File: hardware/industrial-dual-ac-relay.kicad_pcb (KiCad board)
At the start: 2 copper layers, 40 x 40 mm, 29 parts, among them P1 CON-SENSOR, P2 Digital Output, P3 Debug, P4 Boot, U1 XMC1100, U2 AQH3213AX, U5 AQH3213AX, U6 DRILL, U7 DRILL, U8 DRILL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

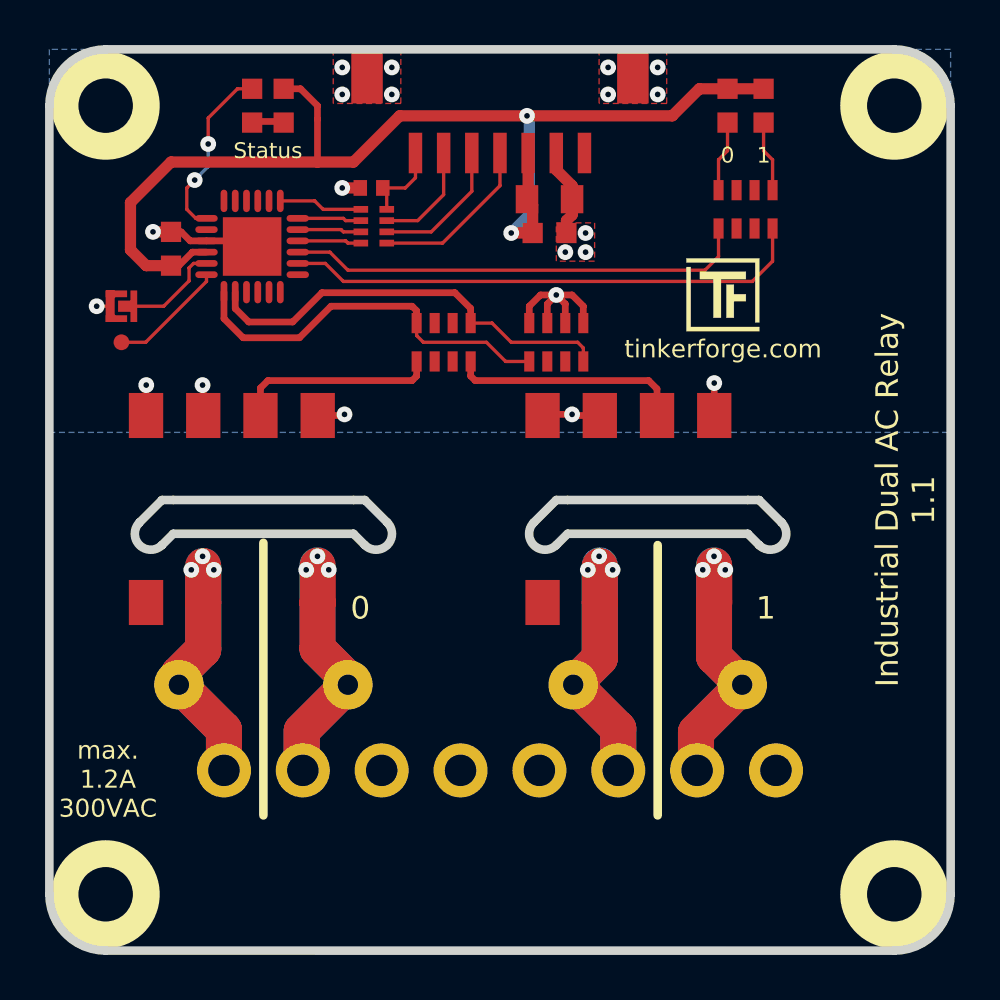
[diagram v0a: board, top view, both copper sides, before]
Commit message: changed to KiCad 6, changed OQ footprint for more clearence
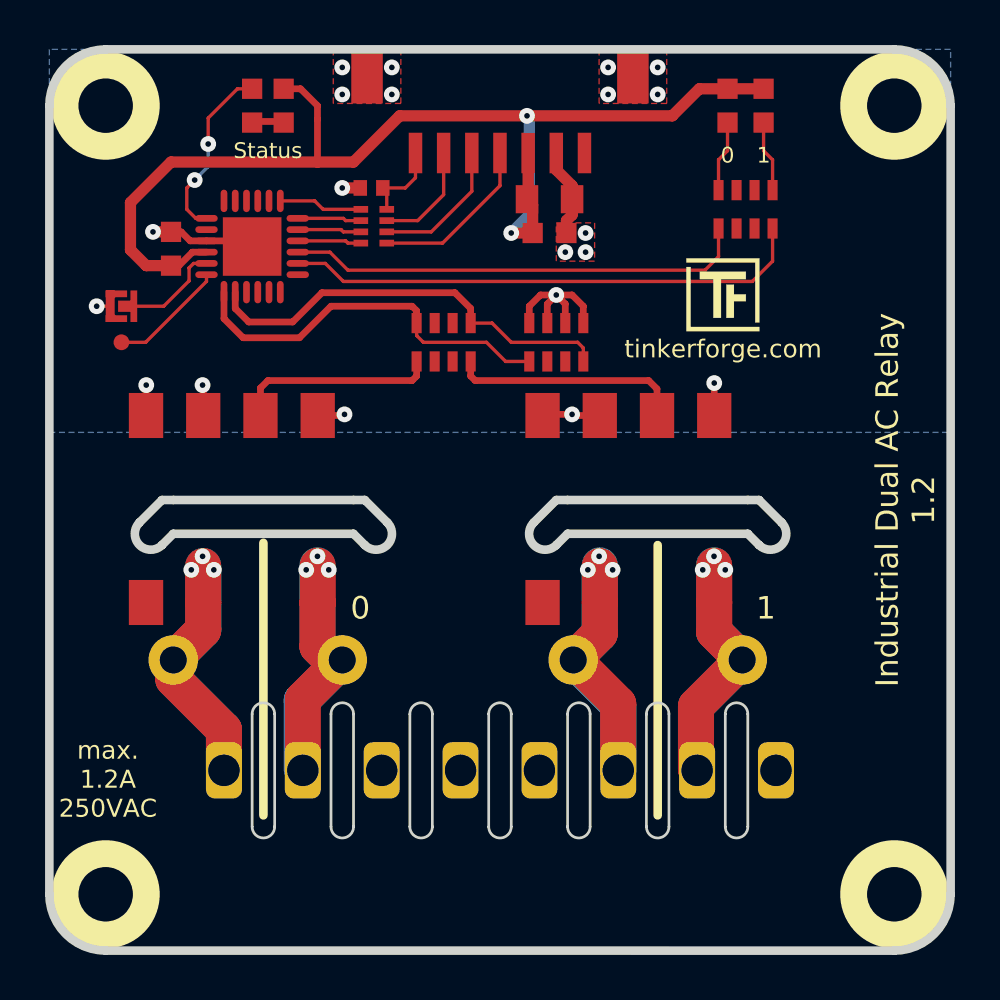
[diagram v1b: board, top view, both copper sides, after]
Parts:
- P2: footprint kicad-libraries:OQ_8P -> kicad-libraries:OQ_8P_230V
- moved R4 1.13 mm to (107.0, 65.2)
- moved R1 1.10 mm to (124.8, 65.2)
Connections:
- P1 pad 1: Net-(P1-Pad1) -> unconnected-(P1-Pad1)
- P2 pad 3: Net-(P2-Pad3) -> unconnected-(P2-Pad3)
- P2 pad 4: Net-(P2-Pad4) -> unconnected-(P2-Pad4)
- P2 pad 5: Net-(P2-Pad5) -> unconnected-(P2-Pad5)
- P2 pad 8: Net-(P2-Pad8) -> unconnected-(P2-Pad8)
- RP1 pad 2: Net-(RP1-Pad2) -> unconnected-(RP1-Pad2)
- RP1 pad 3: Net-(RP1-Pad3) -> unconnected-(RP1-Pad3)
- RP1 pad 6: Net-(RP1-Pad6) -> unconnected-(RP1-Pad6)
- RP1 pad 7: Net-(RP1-Pad7) -> unconnected-(RP1-Pad7)
- RP3 pad 2: Net-(RP3-Pad2) -> unconnected-(RP3-Pad2)
- RP3 pad 3: Net-(RP3-Pad3) -> unconnected-(RP3-Pad3)
- RP3 pad 6: Net-(RP3-Pad6) -> unconnected-(RP3-Pad6)
- RP3 pad 7: Net-(RP3-Pad7) -> unconnected-(RP3-Pad7)
- RP4 pad 2: Net-(RP4-Pad2) -> unconnected-(RP4-Pad2)
- RP4 pad 3: Net-(RP4-Pad3) -> unconnected-(RP4-Pad3)
- U1 pad 15: Net-(U1-Pad15) -> unconnected-(U1-Pad15)
- U1 pad 16: Net-(U1-Pad16) -> unconnected-(U1-Pad16)
- U1 pad 17: Net-(U1-Pad17) -> unconnected-(U1-Pad17)
- U1 pad 18: Net-(U1-Pad18) -> unconnected-(U1-Pad18)
- U1 pad 19: Net-(U1-Pad19) -> unconnected-(U1-Pad19)
- U1 pad 2: Net-(U1-Pad2) -> unconnected-(U1-Pad2)
- U1 pad 3: Net-(U1-Pad3) -> unconnected-(U1-Pad3)
- U1 pad 4: Net-(U1-Pad4) -> unconnected-(U1-Pad4)
- U1 pad 5: Net-(U1-Pad5) -> unconnected-(U1-Pad5)
- U1 pad 6: Net-(U1-Pad6) -> unconnected-(U1-Pad6)
- U1 pad 8: Net-(U1-Pad8) -> unconnected-(U1-Pad8)
- U2 pad 5: Net-(U2-Pad5) -> unconnected-(U2-Pad5)
- U5 pad 5: Net-(U5-Pad5) -> unconnected-(U5-Pad5)
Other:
- net class Default removed
- board text added: "Industrial Dual AC Relay 1.2"
- board text added: "max. 1.2A 250VAC"
- board text removed: "Industrial Dual AC Relay 1.1"
- board text removed: "max. 1.2A 300VAC"

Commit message: changes
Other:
- board text added: "max. 1.2A 230VAC"
- board text removed: "max. 1.2A 250VAC"
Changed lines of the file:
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@@
       (effects (font (size 0.59944 0.59944) (thickness 0.12446)))
     )
-    (fp_line (start 7.5 -2.5) (end 7.5 2.5) (layer "Edge.Cuts") (width 0.12))
+    (fp_line (start 7.5 -5) (end 7.5 2.5) (layer "Edge.Cuts") (width 0.12))
     (fp_line (start 3 -2.5) (end 3 2.5) (layer "Edge.Cuts") (width 0.12))
     (fp_line (start 11 -2.5) (end 11 2.5) (layer "Edge.Cuts") (width 0.12))
     (fp_line (start 0.5 -2.5) (end 0.5 2.5) (layer "Edge.Cuts") (width 0.12))
-    (fp_line (start -10 -2.5) (end -10 2.5) (layer "Edge.Cuts") (width 0.12))
+    (fp_line (start -10 -5) (end -10 2.5) (layer "Edge.Cuts") (width 0.12))
     (fp_line (start 4 -2.5) (end 4 2.5) (layer "Edge.Cuts") (width 0.12))
-    (fp_line (start 6.5 -2.5) (end 6.5 2.5) (layer "Edge.Cuts") (width 0.12))
+    (fp_line (start 6.5 -5) (end 6.5 2.5) (layer "Edge.Cuts") (width 0.12))
     (fp_line (start -4 -2.5) (end -4 2.5) (layer "Edge.Cuts") (width 0.12))
     (fp_line (start -6.5 -2.5) (end -6.5 2.5) (layer "Edge.Cuts") (width 0.12))
     (fp_line (start 10 -2.5) (end 10 2.5) (layer "Edge.Cuts") (width 0.12))
-    (fp_line (start -11 -2.5) (end -11 2.5) (layer "Edge.Cuts") (width 0.12))
+    (fp_line (start -11 -5) (end -11 2.5) (layer "Edge.Cuts") (width 0.12))
     (fp_line (start -7.5 -2.5) (end -7.5 2.5) (layer "Edge.Cuts") (width 0.12))
     (fp_line (start -0.5 -2.5) (end -0.5 2.5) (layer "Edge.Cuts") (width 0.12))
@@
     (fp_arc (start 11 2.5) (mid 10.5 3) (end 10 2.5) (layer "Edge.Cuts") (width 0.12))
     (fp_arc (start -7.5 -2.5) (mid -7 -3) (end -6.5 -2.5) (layer "Edge.Cuts") (width 0.12))
-    (fp_arc (start -11 -2.5) (mid -10.5 -3) (end -10 -2.5) (layer "Edge.Cuts") (width 0.12))
-    (fp_arc (start 6.5 -2.5) (mid 7 -3) (end 7.5 -2.5) (layer "Edge.Cuts") (width 0.12))
+    (fp_arc (start -11 -5) (mid -10.5 -5.5) (end -10 -5) (layer "Edge.Cuts") (width 0.12))
+    (fp_arc (start 6.5 -5) (mid 7 -5.5) (end 7.5 -5) (layer "Edge.Cuts") (width 0.12))
     (fp_arc (start -6.5 2.5) (mid -7 3) (end -7.5 2.5) (layer "Edge.Cuts") (width 0.12))
     (fp_arc (start 7.5 2.5) (mid 7 3) (end 6.5 2.5) (layer "Edge.Cuts") (width 0.12))
@@
     (effects (font (size 0.70104 0.70104) (thickness 0.14986)))
   )
-  (gr_text "max.\n1.2A\n250VAC\n" (at 100.4 70.45) (layer "F.SilkS")
+  (gr_text "max.\n1.2A\n230VAC\n" (at 100.4 70.45) (layer "F.SilkS")
     (effects (font (size 0.8 0.8) (thickness 0.15)))
   )

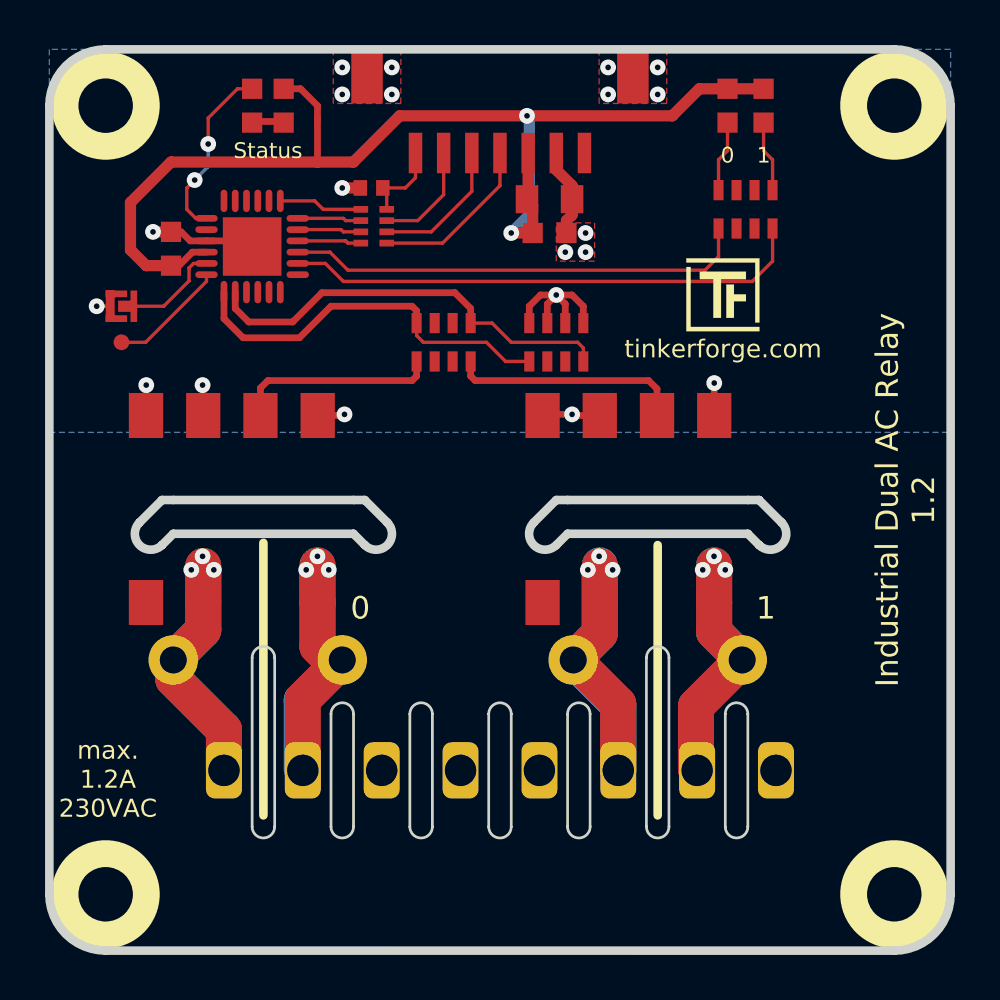
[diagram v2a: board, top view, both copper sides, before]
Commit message: extented the clearance slits
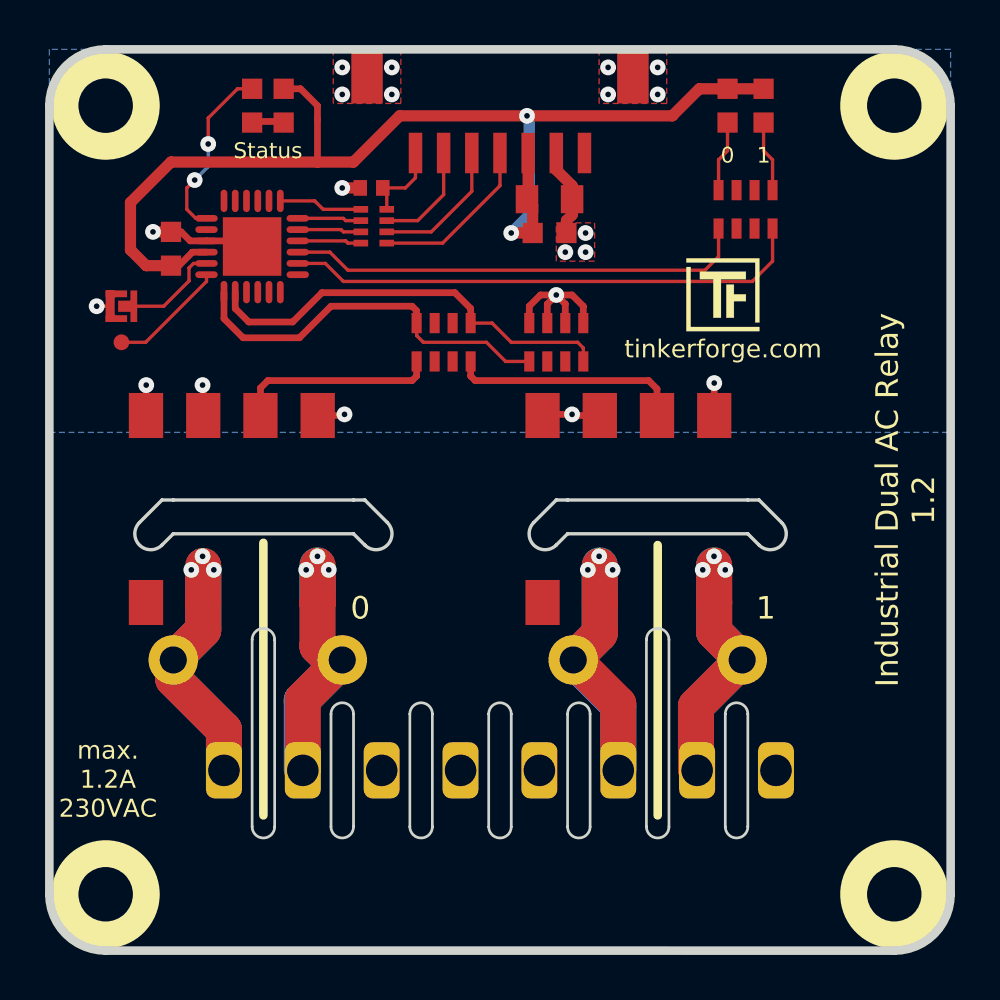
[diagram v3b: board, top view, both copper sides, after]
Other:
- board text added: "AQH3213AX"
- board text added: "U5"
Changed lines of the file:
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@@
       (effects (font (size 0.59944 0.59944) (thickness 0.12446)))
     )
-    (fp_line (start 7.5 -5) (end 7.5 2.5) (layer "Edge.Cuts") (width 0.12))
+    (fp_line (start 7.5 -5.8) (end 7.5 2.5) (layer "Edge.Cuts") (width 0.12))
     (fp_line (start 3 -2.5) (end 3 2.5) (layer "Edge.Cuts") (width 0.12))
     (fp_line (start 11 -2.5) (end 11 2.5) (layer "Edge.Cuts") (width 0.12))
     (fp_line (start 0.5 -2.5) (end 0.5 2.5) (layer "Edge.Cuts") (width 0.12))
-    (fp_line (start -10 -5) (end -10 2.5) (layer "Edge.Cuts") (width 0.12))
+    (fp_line (start -10 -5.8) (end -10 2.5) (layer "Edge.Cuts") (width 0.12))
     (fp_line (start 4 -2.5) (end 4 2.5) (layer "Edge.Cuts") (width 0.12))
-    (fp_line (start 6.5 -5) (end 6.5 2.5) (layer "Edge.Cuts") (width 0.12))
+    (fp_line (start 6.5 -5.8) (end 6.5 2.5) (layer "Edge.Cuts") (width 0.12))
     (fp_line (start -4 -2.5) (end -4 2.5) (layer "Edge.Cuts") (width 0.12))
     (fp_line (start -6.5 -2.5) (end -6.5 2.5) (layer "Edge.Cuts") (width 0.12))
     (fp_line (start 10 -2.5) (end 10 2.5) (layer "Edge.Cuts") (width 0.12))
-    (fp_line (start -11 -5) (end -11 2.5) (layer "Edge.Cuts") (width 0.12))
+    (fp_line (start -11 -5.8) (end -11 2.5) (layer "Edge.Cuts") (width 0.12))
     (fp_line (start -7.5 -2.5) (end -7.5 2.5) (layer "Edge.Cuts") (width 0.12))
     (fp_line (start -0.5 -2.5) (end -0.5 2.5) (layer "Edge.Cuts") (width 0.12))
@@
     (fp_arc (start 11 2.5) (mid 10.5 3) (end 10 2.5) (layer "Edge.Cuts") (width 0.12))
     (fp_arc (start -7.5 -2.5) (mid -7 -3) (end -6.5 -2.5) (layer "Edge.Cuts") (width 0.12))
-    (fp_arc (start -11 -5) (mid -10.5 -5.5) (end -10 -5) (layer "Edge.Cuts") (width 0.12))
-    (fp_arc (start 6.5 -5) (mid 7 -5.5) (end 7.5 -5) (layer "Edge.Cuts") (width 0.12))
+    (fp_arc (start -11 -5.8) (mid -10.5 -6.3) (end -10 -5.8) (layer "Edge.Cuts") (width 0.12))
+    (fp_arc (start 6.5 -5.8) (mid 7 -6.3) (end 7.5 -5.8) (layer "Edge.Cuts") (width 0.12))
     (fp_arc (start -6.5 2.5) (mid -7 3) (end -7.5 2.5) (layer "Edge.Cuts") (width 0.12))
     (fp_arc (start 7.5 2.5) (mid 7 3) (end 6.5 2.5) (layer "Edge.Cuts") (width 0.12))
@@
     (property "Sheetname" "")
     (attr through_hole)
-    (fp_text reference "U2" (at 0 0.5) (layer "F.Fab")
+    (fp_text reference "U2" (at -5.95 -0.95) (layer "F.Fab")
       (effects (font (size 0.25 0.25) (thickness 0.0625)))
     )
-    (fp_text value "AQH3213AX" (at 0 -0.5) (layer "F.Fab")
+    (fp_text value "AQH3213AX" (at -5.95 -1.95) (layer "F.Fab")
       (effects (font (size 0.25 0.25) (thickness 0.0625)))
     )
@@
   (gr_line (start 124.8 72.05) (end 124.8 60.05) (layer "F.SilkS") (width 0.381))
   (gr_line (start 107.3 72.05) (end 107.3 59.95) (layer "F.SilkS") (width 0.381))
-  (gr_line (start 120.8 58.05) (end 128.8 58.05) (layer "Edge.Cuts") (width 0.381))
-  (gr_line (start 120.3 58.05) (end 119.3 59.05) (layer "Edge.Cuts") (width 0.381))
-  (gr_line (start 120.8 58.05) (end 120.3 58.05) (layer "Edge.Cuts") (width 0.381))
-  (gr_line (start 128.8 59.55) (end 129.3 60.05) (layer "Edge.Cuts") (width 0.381))
-  (gr_line (start 128.8 58.05) (end 129.3 58.05) (layer "Edge.Cuts") (width 0.381))
-  (gr_line (start 120.8 59.55) (end 120.3 60.05) (layer "Edge.Cuts") (width 0.381))
-  (gr_line (start 120.8 59.55) (end 128.8 59.55) (layer "Edge.Cuts") (width 0.381))
-  (gr_arc (start 130.299999 59.050001) (mid 130.299999 60.049999) (end 129.300001 60.049999) (layer "Edge.Cuts") (width 0.381))
-  (gr_line (start 129.3 58.05) (end 130.3 59.05) (layer "Edge.Cuts") (width 0.381))
-  (gr_arc (start 120.299999 60.049999) (mid 119.300001 60.049999) (end 119.300001 59.050001) (layer "Edge.Cuts") (width 0.381))
   (gr_arc (start 97.80016 40.5511) (mid 98.532206 38.783786) (end 100.29952 38.05174) (layer "Edge.Cuts") (width 0.381))
-  (gr_line (start 103.3 59.55) (end 111.3 59.55) (layer "Edge.Cuts") (width 0.381))
-  (gr_line (start 111.3 59.55) (end 111.8 60.05) (layer "Edge.Cuts") (width 0.381))
-  (gr_line (start 103.3 58.05) (end 102.8 58.05) (layer "Edge.Cuts") (width 0.381))
-  (gr_line (start 102.8 58.05) (end 101.8 59.05) (layer "Edge.Cuts") (width 0.381))
-  (gr_line (start 103.3 59.55) (end 102.8 60.05) (layer "Edge.Cuts") (width 0.381))
+  (gr_line (start 103.3 59.55) (end 111.3 59.55) (layer "Edge.Cuts") (width 0.15))
+  (gr_line (start 111.3 59.55) (end 111.8 60.05) (layer "Edge.Cuts") (width 0.15))
+  (gr_line (start 129.3 58.05) (end 130.3 59.05) (layer "Edge.Cuts") (width 0.15))
+  (gr_line (start 103.3 58.05) (end 102.8 58.05) (layer "Edge.Cuts") (width 0.15))
+  (gr_line (start 102.8 58.05) (end 101.8 59.05) (layer "Edge.Cuts") (width 0.15))
+  (gr_line (start 103.3 59.55) (end 102.8 60.05) (layer "Edge.Cuts") (width 0.15))
   (gr_line (start 97.80016 40.5511) (end 97.8 75.54976) (layer "Edge.Cuts") (width 0.381))
   (gr_line (start 100.29952 78.04912) (end 135.29818 78.05166) (layer "Edge.Cuts") (width 0.381))
   (gr_arc (start 135.29818 38.0492) (mid 137.06729 38.78199) (end 137.80008 40.5511) (layer "Edge.Cuts") (width 0.381))
-  (gr_line (start 103.3 58.05) (end 111.3 58.05) (layer "Edge.Cuts") (width 0.381))
-  (gr_line (start 111.3 58.05) (end 111.8 58.05) (layer "Edge.Cuts") (width 0.381))
-  (gr_line (start 111.8 58.05) (end 112.8 59.05) (layer "Edge.Cuts") (width 0.381))
+  (gr_line (start 103.3 58.05) (end 111.3 58.05) (layer "Edge.Cuts") (width 0.15))
+  (gr_line (start 111.3 58.05) (end 111.8 58.05) (layer "Edge.Cuts") (width 0.15))
+  (gr_line (start 128.8 58.05) (end 129.3 58.05) (layer "Edge.Cuts") (width 0.15))
+  (gr_line (start 111.8 58.05) (end 112.8 59.05) (layer "Edge.Cuts") (width 0.15))
+  (gr_line (start 120.8 59.55) (end 128.8 59.55) (layer "Edge.Cuts") (width 0.15))
+  (gr_line (start 128.8 59.55) (end 129.3 60.05) (layer "Edge.Cuts") (width 0.15))
   (gr_arc (start 100.29952 78.04912) (mid 98.532206 77.317074) (end 97.80016 75.54976) (layer "Edge.Cuts") (width 0.381))
+  (gr_line (start 120.8 58.05) (end 128.8 58.05) (layer "Edge.Cuts") (width 0.15))
+  (gr_line (start 120.3 58.05) (end 119.3 59.05) (layer "Edge.Cuts") (width 0.15))
   (gr_arc (start 137.80008 75.54976) (mid 137.06729 77.31887) (end 135.29818 78.05166) (layer "Edge.Cuts") (width 0.381))
-  (gr_arc (start 102.799999 60.049999) (mid 101.800001 60.049999) (end 101.800001 59.050001) (layer "Edge.Cuts") (width 0.381))
-  (gr_arc (start 112.799999 59.050001) (mid 112.799999 60.049999) (end 111.800001 60.049999) (layer "Edge.Cuts") (width 0.381))
+  (gr_arc (start 102.799999 60.049999) (mid 101.800001 60.049999) (end 101.800001 59.050001) (layer "Edge.Cuts") (width 0.15))
+  (gr_line (start 120.8 59.55) (end 120.3 60.05) (layer "Edge.Cuts") (width 0.15))
+  (gr_arc (start 112.799999 59.050001) (mid 112.799999 60.049999) (end 111.800001 60.049999) (layer "Edge.Cuts") (width 0.15))
+  (gr_arc (start 130.299999 59.050001) (mid 130.299999 60.049999) (end 129.300001 60.049999) (layer "Edge.Cuts") (width 0.15))
   (gr_line (start 135.30072 38.0492) (end 100.29952 38.0492) (layer "Edge.Cuts") (width 0.381))
   (gr_line (start 137.80262 75.54976) (end 137.80262 40.5511) (layer "Edge.Cuts") (width 0.381))
+  (gr_arc (start 120.299999 60.049999) (mid 119.300001 60.049999) (end 119.300001 59.050001) (layer "Edge.Cuts") (width 0.15))
+  (gr_line (start 120.8 58.05) (end 120.3 58.05) (layer "Edge.Cuts") (width 0.15))
   (gr_text "0" (at 107.4 76.65) (layer "B.SilkS")
     (effects (font (size 1.00076 1.00076) (thickness 0.14986)))
@@
     (effects (font (size 0.8001 0.8001) (thickness 0.200025)))
   )
+  (gr_text "AQH3213AX" (at 123.4 58.95 -180) (layer "F.Fab")
+    (effects (font (size 0.25 0.25) (thickness 0.0625)))
+  )
+  (gr_text "U5" (at 123.4 57.95 -180) (layer "F.Fab")
+    (effects (font (size 0.25 0.25) (thickness 0.0625)))
+  )
   (segment (start 104.15 47.05) (end 103.55 47.65) (width 0.29972) (layer "F.Cu") (net 1))

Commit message: Prototype V1.2
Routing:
- net GND: track 30.0 -> 32.6 mm
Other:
- outline, holes or cut-outs redrawn
